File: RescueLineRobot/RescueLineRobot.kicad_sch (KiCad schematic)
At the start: 8 parts, among them J1 Conn_01x11, J2 Bateria, J3 Motor 1, J4 Motor 2, J5 Convertidor, U1 ROB-14450, U2 ESP32-DEVKIT-V1

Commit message: updates
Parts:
- added J6: Laser 1, Connector_JST:JST_XH_B4B-XH-A_1x04_P2.50mm_Vertical, symbol Connector_Generic:Conn_01x04
- added J7: Laser 2, Connector_JST:JST_XH_B4B-XH-A_1x04_P2.50mm_Vertical, symbol Connector_Generic:Conn_01x04
- added J8: Laser 3, Connector_JST:JST_XH_B4B-XH-A_1x04_P2.50mm_Vertical, symbol Connector_Generic:Conn_01x04
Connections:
- net at J1.1 (Pin_1), J2.1 (Pin_1), J5.2 (Pin_2)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: now also J6.2 (Pin_2), J7.2 (Pin_2), J8.2 (Pin_2)
- net at J1.11 (Pin_11), J5.1 (Pin_1), U2.30 (VIN): now also J6.1 (Pin_1), J7.1 (Pin_1), J8.1 (Pin_1)
- net at U2.11 (D21): now also J6.4 (Pin_4), J7.4 (Pin_4), J8.4 (Pin_4)
- net at U2.14 (D22): now also J6.3 (Pin_3), J7.3 (Pin_3), J8.3 (Pin_3)
- net at U2.17 (VP): now also J1.9 (Pin_9); no longer J1.10 (Pin_10)
- net at U2.18 (VN): now also J1.10 (Pin_10); no longer J1.9 (Pin_9)

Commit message: Motores funcionan :D
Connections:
- net at U1.10 (PWMB): now also U2.10 (D19); no longer U2.9 (D18)
- net at U1.11 (BI2): now also U2.9 (D18); no longer U2.5 (D4)
- net at U1.14 (AI1): now also U2.7 (TX2); no longer U2.26 (D14)
- net at U1.15 (AI2): now also U2.6 (RX2); no longer U2.28 (D13)
- net at U1.16 (PWMA): now also U2.5 (D4); no longer U2.10 (D19)
- net at U2.17 (VP): now also J1.10 (Pin_10); no longer J1.9 (Pin_9)
- net at U2.18 (VN): now also J1.9 (Pin_9); no longer J1.10 (Pin_10)

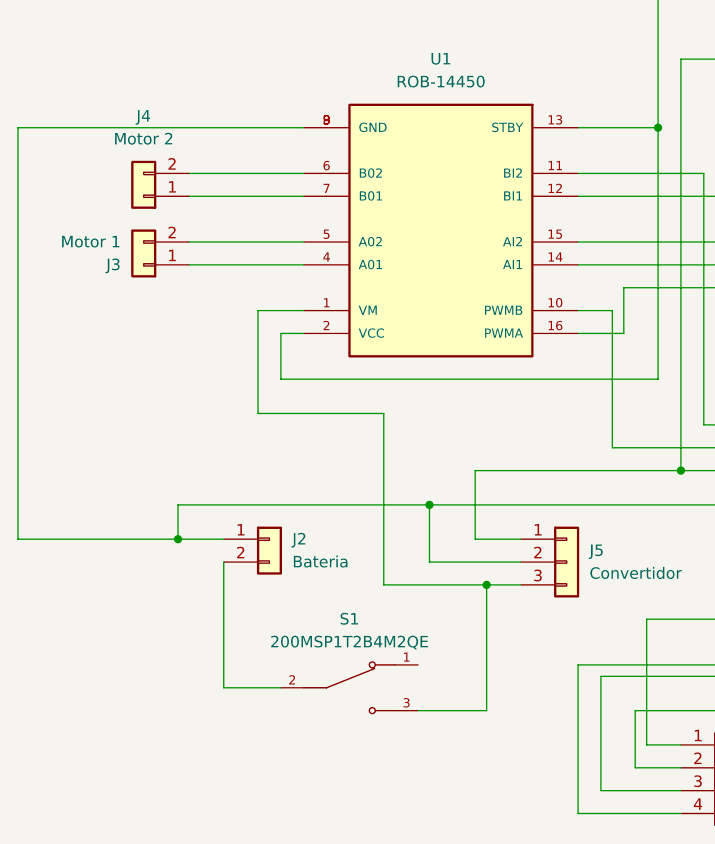
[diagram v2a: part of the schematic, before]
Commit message: Actualizacion de pcb
Ahora la pcb está más limpia y con serigrafía
Pendientes:
-2 Sensores RGB
-1 Botón pulsador
-2 Encoders para los motores (aun no se si cuadraticos o no)
-1 Puerto para servo (maybe con selector de voltaje)
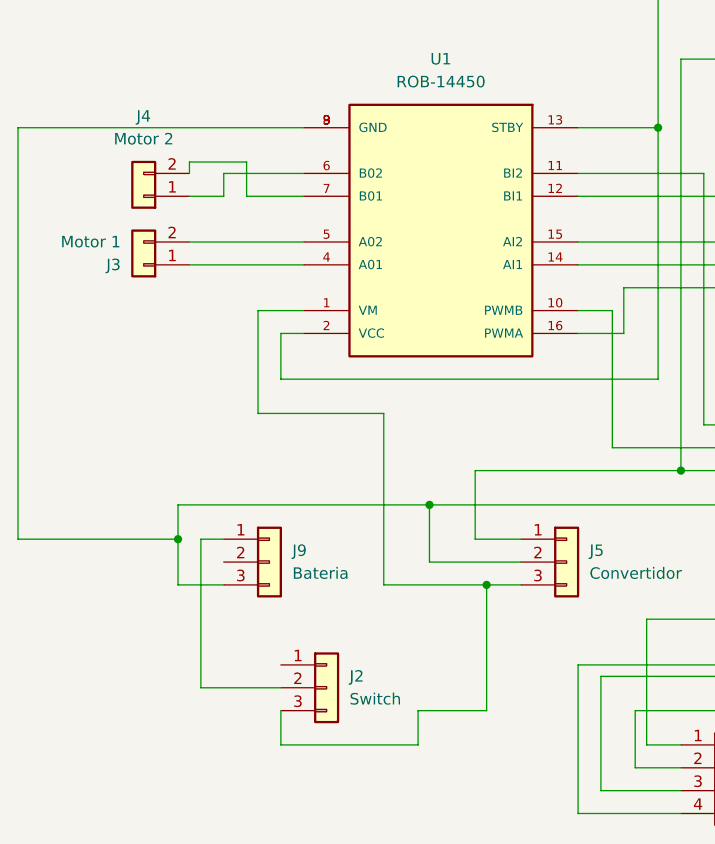
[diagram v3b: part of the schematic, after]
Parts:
- removed J2: Bateria, Connector_JST:JST_XH_B2B-XH-A_1x02_P2.50mm_Vertical, symbol Connector_Generic:Conn_01x02
- removed S1: 200MSP1T2B4M2QE, 200MSP1T2B4M2QE:SW_200MSP1T2B4M2QE, symbol 200MSP1T2B4M2QE:200MSP1T2B4M2QE
- added J2: Switch, Connector_JST:JST_XH_B3B-XH-A_1x03_P2.50mm_Vertical, symbol Connector_Generic:Conn_01x03
- added J9: Bateria, Connector_JST:JST_XH_B3B-XH-A_1x03_P2.50mm_Vertical, symbol Connector_Generic:Conn_01x03
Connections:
- net at J1.1 (Pin_1), J5.2 (Pin_2), J6.2 (Pin_2)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: now also J9.3 (Pin_3)
- net at J4.1 (Pin_1): now also U1.6 (B02); no longer U1.7 (B01)
- net at J4.2 (Pin_2): now also U1.7 (B01); no longer U1.6 (B02)
- net at J5.3 (Pin_3), U1.1 (VM): now also J2.3 (Pin_3)
- new net: J2.2 (Pin_2), J9.1 (Pin_1)

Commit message: Boton y encoders
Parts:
- added Boton1: SW_Push, Button_Switch_THT:SW_PUSH-12mm, symbol Switch:SW_Push
- added EncoderA1: Encoder A, Connector_JST:JST_XA_B03B-XASK-1_1x03_P2.50mm_Vertical, symbol Connector_Generic:Conn_01x03
- added EncoderB1: Encoder B, Connector_JST:JST_XA_B03B-XASK-1_1x03_P2.50mm_Vertical, symbol Connector_Generic:Conn_01x03
- added Resistencia1: R, Resistor_THT:R_Axial_DIN0617_L17.0mm_D6.0mm_P25.40mm_Horizontal, symbol Device:R
- MotorB1: renamed from J4; value Motor 2 -> MotorB
- renumbered J9 to Bateria1, J5 to Convertidor1, U2 to Esp32, J6 to Laser1, J7 to Laser2, J8 to Laser3, J3 to MotorA1, J1 to SigueLineas1, J2 to Switch1, U1 to TB6612FNG1
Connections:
- net at Convertidor1.1 (Pin_1), Esp32.30 (VIN), Laser1.1 (Pin_1)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: now also Boton1.2, EncoderA1.3 (Pin_3), EncoderB1.3 (Pin_3)
- net at Bateria1.3 (Pin_3), Convertidor1.2 (Pin_2), Esp32.2 (GND)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: now also EncoderA1.1 (Pin_1), EncoderB1.1 (Pin_1), Resistencia1.1
- net at Esp32.26 (D14): now also EncoderB1.2 (Pin_2)
- net at Esp32.27 (D12): now also Boton1.1, Resistencia1.2
- net at Esp32.28 (D13): now also EncoderA1.2 (Pin_2)

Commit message: Estamos Casi
Están todas las rutas hechas, todos los puertos necesarios, sólo falta nombrar al robot y poner gráficas
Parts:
- added I2C1, I2C2, RGB1, RGB2: ~, Connector_JST:JST_XH_B4B-XH-A_1x04_P2.50mm_Vertical, symbol Connector_Generic:Conn_01x04
- added SERVO1: Conn_01x03, Connector_JST:JST_XH_B3B-XH-A_1x03_P2.50mm_Vertical, symbol Connector_Generic:Conn_01x03
- added SERVOPOWER1: Conn_01x03, Connector_PinHeader_1.27mm:PinHeader_1x03_P1.27mm_Vertical, symbol Connector_Generic:Conn_01x03
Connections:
- net 5V: now reaches Boton1.2, Convertidor1.1 (Pin_1), EncoderA1.3 (Pin_3), EncoderB1.3 (Pin_3), Esp32.30 (VIN), Laser1.1 (Pin_1), Laser2.1 (Pin_1), Laser3.1 (Pin_1), SigueLineas1.11 (Pin_11)
- net 5V: now also I2C1.1 (Pin_1), I2C2.1 (Pin_1), RGB1.1 (Pin_1), RGB2.1 (Pin_1), SERVOPOWER1.1 (Pin_1)
- net GND: now reaches Bateria1.3 (Pin_3), Convertidor1.2 (Pin_2), EncoderA1.1 (Pin_1), EncoderB1.1 (Pin_1), Esp32.2 (GND), Esp32.29 (GND), Laser1.2 (Pin_2), Laser2.2 (Pin_2), Laser3.2 (Pin_2), Resistencia1.1, SigueLineas1.1 (Pin_1), TB6612FNG1.3 (GND), TB6612FNG1.8 (GND), TB6612FNG1.9 (GND)
- net GND: now also I2C1.2 (Pin_2), I2C2.2 (Pin_2), RGB1.2 (Pin_2), RGB2.2 (Pin_2), SERVO1.1 (Pin_1)
- net D22: now reaches Esp32.14 (D22), Laser1.3 (Pin_3), Laser2.3 (Pin_3), Laser3.3 (Pin_3)
- net D22: now also I2C1.3 (Pin_3), I2C2.3 (Pin_3), RGB1.3 (Pin_3), RGB2.3 (Pin_3)
- net D21: now reaches Esp32.11 (D21), Laser1.4 (Pin_4), Laser2.4 (Pin_4), Laser3.4 (Pin_4)
- net D21: now also I2C1.4 (Pin_4), I2C2.4 (Pin_4), RGB1.4 (Pin_4), RGB2.4 (Pin_4)
- net 7V4: now reaches Convertidor1.3 (Pin_3), Switch1.3 (Pin_3), TB6612FNG1.1 (VM)
- net 7V4: now also SERVOPOWER1.3 (Pin_3)
- net D19: now reaches Esp32.10 (D19), TB6612FNG1.10 (PWMB)
- net D18: now reaches Esp32.9 (D18), TB6612FNG1.11 (BI2)
- net D5: now reaches Esp32.8 (D5), TB6612FNG1.12 (BI1)
- net 3V3: now reaches Esp32.1 (3V3), TB6612FNG1.13 (STBY), TB6612FNG1.2 (VCC)
- net D17: now reaches Esp32.7 (TX2), TB6612FNG1.14 (AI1)
- net D16: now reaches Esp32.6 (RX2), TB6612FNG1.15 (AI2)
- net D4: now reaches Esp32.5 (D4), TB6612FNG1.16 (PWMA)
- net D12: now reaches Boton1.1, Resistencia1.2
- net D12: now also Esp32.26 (D14); no longer Esp32.27 (D12)
- net VIN: now reaches Bateria1.1 (Pin_1), Switch1.2 (Pin_2)
- net D14: now reaches EncoderB1.2 (Pin_2)
- net D14: now also Esp32.3 (D15); no longer Esp32.26 (D14)
- net D23: now reaches Esp32.15 (D23)
- net D23: now also SERVO1.3 (Pin_3)
- net D36: now reaches Esp32.17 (VP), SigueLineas1.10 (Pin_10)
- net D39: now reaches Esp32.18 (VN), SigueLineas1.9 (Pin_9)
- net D34: now reaches Esp32.19 (D34), SigueLineas1.8 (Pin_8)
- net D35: now reaches Esp32.20 (D35), SigueLineas1.7 (Pin_7)
- net D32: now reaches Esp32.21 (D32), SigueLineas1.6 (Pin_6)
- net D33: now reaches Esp32.22 (D33), SigueLineas1.5 (Pin_5)
- net D25: now reaches Esp32.23 (D25), SigueLineas1.4 (Pin_4)
- net D26: now reaches Esp32.24 (D26), SigueLineas1.3 (Pin_3)
- net D27: now reaches Esp32.25 (D27), SigueLineas1.2 (Pin_2)
- net D13: now reaches EncoderA1.2 (Pin_2), Esp32.28 (D13)
- new net ServoV: SERVO1.2 (Pin_2), SERVOPOWER1.2 (Pin_2)
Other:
- moved on the sheet: Bateria1, Boton1, Convertidor1, EncoderA1, EncoderB1, Esp32, Laser1, Laser2, Laser3, MotorA1, MotorB1, Resistencia1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

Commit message: Dynamis a nacido
Estamos listos señores!!!
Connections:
- net D12: now also Esp32.27 (D12); no longer Esp32.26 (D14)
- net D14: now also Esp32.26 (D14); no longer Esp32.3 (D15)
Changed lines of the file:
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@@
-	(wire
-		(pts
-			(xy 125.73 53.34) (xy 127 53.34)
-		)
-		(stroke
-			(width 0)
-			(type default)
-		)
-	)
 	(wire
 		(pts
@@
 	(global_label "D14"
 		(shape bidirectional)
-		(at 95.25 68.58 180)
-		(fields_autoplaced yes)
-		(effects
-			(font
-				(size 1.27 1.27)
-			)
-			(justify right)
-		)
-		(property "Intersheetrefs" "${INTERSHEET_REFS}"
-			(at 87.4645 68.58 0)
+		(at 95.25 66.04 180)
+		(fields_autoplaced yes)
+		(effects
+			(font
+				(size 1.27 1.27)
+			)
+			(justify right)
+		)
+		(property "Intersheetrefs" "${INTERSHEET_REFS}"
+			(at 87.4645 66.04 0)
 			(effects
 				(font
@@
 	(global_label "D22"
 		(shape bidirectional)
-		(at 127 53.34 0)
+		(at 125.73 53.34 0)
 		(fields_autoplaced yes)
 		(effects
@@
 		)
 		(property "Intersheetrefs" "${INTERSHEET_REFS}"
-			(at 134.7855 53.34 0)
+			(at 133.5155 53.34 0)
 			(effects
 				(font
@@
 	(global_label "D12"
 		(shape bidirectional)
-		(at 95.25 66.04 180)
-		(fields_autoplaced yes)
-		(effects
-			(font
-				(size 1.27 1.27)
-			)
-			(justify right)
-		)
-		(property "Intersheetrefs" "${INTERSHEET_REFS}"
-			(at 87.4645 66.04 0)
-			(effects
-				(font
+		(at 95.25 60.96 180)
+		(fields_autoplaced yes)
+		(effects
+			(font
+				(size 1.27 1.27)
+			)
+			(justify right)
+		)
+		(property "Intersheetrefs" "${INTERSHEET_REFS}"
+			(at 87.4645 60.96 0)
+			(effects
+				(font

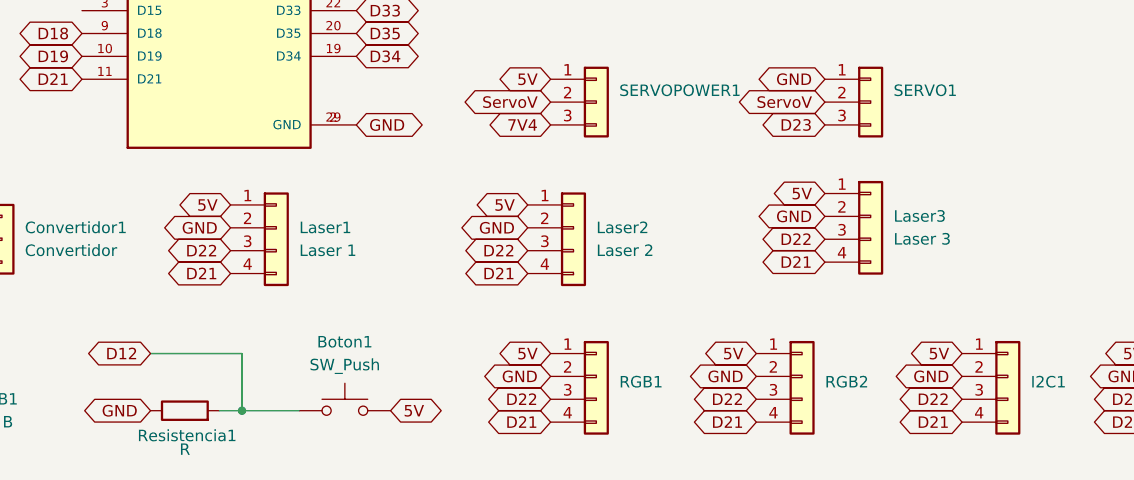
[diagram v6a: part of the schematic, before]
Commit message: Dynamis V2
- Sólo 4 i2c en la placa
- Cambiar serigrafía de los motores hacia el lado superior
- Agrandar puenteo para el voltaje del servo
- Rotar conector de QTR hacia el lado más largo de la placa
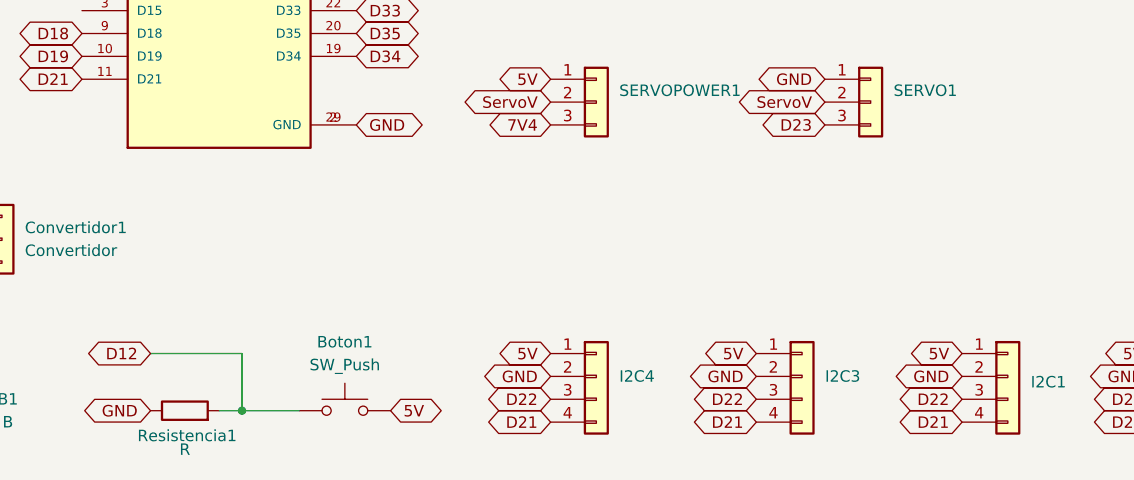
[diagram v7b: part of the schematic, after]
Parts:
- removed Laser1: Laser 1, Connector_JST:JST_XH_B4B-XH-A_1x04_P2.50mm_Vertical, symbol Connector_Generic:Conn_01x04
- removed Laser2: Laser 2, Connector_JST:JST_XH_B4B-XH-A_1x04_P2.50mm_Vertical, symbol Connector_Generic:Conn_01x04
- removed Laser3: Laser 3, Connector_JST:JST_XH_B4B-XH-A_1x04_P2.50mm_Vertical, symbol Connector_Generic:Conn_01x04
- SERVOPOWER1: footprint Connector_PinHeader_1.27mm:PinHeader_1x03_P1.27mm_Vertical -> Connector_PinHeader_2.54mm:PinHeader_1x03_P2.54mm_Vertical
- renumbered RGB2 to I2C3, RGB1 to I2C4

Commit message: Arreglo regulador de voltaje
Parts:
- Convertidor1: footprint Connector_PinHeader_2.54mm:PinHeader_1x03_P2.54mm_Vertical -> Connector_PinHeader_2.54mm:PinHeader_2x03_P2.54mm_Vertical; symbol Connector_Generic:Conn_01x03 -> Connector_Generic:Conn_02x03_Counter_Clockwise
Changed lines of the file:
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@@
 	)
 	(symbol
-		(lib_id "Connector_Generic:Conn_01x03")
+		(lib_id "Connector_Generic:Conn_02x03_Counter_Clockwise")
 		(at 86.36 93.98 0)
 		(unit 1)
@@
 		(fields_autoplaced yes)
 		(property "Reference" "Convertidor1"
-			(at 88.9 92.7099 0)
+			(at 87.63 85.09 0)
 			(effects
 				(font
 					(size 1.27 1.27)
 				)
-				(justify left)
 			)
 		)
 		(property "Value" "Convertidor"
-			(at 88.9 95.2499 0)
+			(at 87.63 87.63 0)
 			(effects
 				(font
 					(size 1.27 1.27)
 				)
-				(justify left)
 			)
 		)
-		(property "Footprint" "Connector_PinHeader_2.54mm:PinHeader_1x03_P2.54mm_Vertical"
+		(property "Footprint" "Connector_PinHeader_2.54mm:PinHeader_2x03_P2.54mm_Vertical"
 			(at 86.36 93.98 0)
 			(effects
@@
 			)
 		)
-		(property "Description" "Generic connector, single row, 01x03, script generated (kicad-library-utils/schlib/autogen/connector/)"
+		(property "Description" "Generic connector, double row, 02x03, counter clockwise pin numbering scheme (similar to DIP package numbering), script generated (kicad-library-utils/schlib/autogen/connector/)"
 			(at 86.36 93.98 0)
 			(effects
@@
 		(pin "3"
 		)
+		(pin "6"
+		)
+		(pin "4"
+		)
+		(pin "5"
+		)
 		(instances
